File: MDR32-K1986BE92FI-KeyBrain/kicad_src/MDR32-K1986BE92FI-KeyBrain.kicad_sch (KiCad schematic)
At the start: 33 parts, among them J1 USB-C USB 2.0 MC-372, J2 Conn_01x04, U1 AP2112K-3.3, U2 USBLC6-2SC6, U3 K1986BE92FI, U4 ProMicro, Y1 8MHz

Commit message: MDR32-K1986BE92FI-KeyBrain: add usb fottprint
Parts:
- J1: footprint nrfmicro:USB-C_C168688 -> MDR32-K1986BE92FI-KeyBrain:USB-C_C168688
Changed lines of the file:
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@@
 			)
 		)
-		(property "Footprint" "nrfmicro:USB-C_C168688"
+		(property "Footprint" "MDR32-K1986BE92FI-KeyBrain:USB-C_C168688"
 			(at 31.9278 22.225 0)
 			(show_name no)

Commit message: MDR32-K1986BE92FI-KeyBrain: фикс символа кристалла
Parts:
- removed Y1: 8MHz, Crystal:Crystal_SMD_3225-4Pin_3.2x2.5mm, symbol MDR32-K1986BE92FI-DK:Crystal_GND24
- added Y1: 8MHz, Crystal:Crystal_SMD_3225-4Pin_3.2x2.5mm, symbol MDR32-K1986BE92FI-KeyBrain:Crystal_GND24
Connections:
- net GND: now also Y1.2 (G), Y1.4 (G)
- net OSC_IN: now also Y1.1
- net OSC_OUT: now also Y1.3
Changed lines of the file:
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@@
 	)
 	(junction
-		(at 78.74 127)
-		(diameter 0)
-		(color 0 0 0 0)
-	)
-	(junction
 		(at 46.99 44.45)
 		(diameter 0)
@@
 	(wire
 		(pts
-			(xy 78.74 125.73) (xy 78.74 127)
+			(xy 78.74 125.73) (xy 78.74 133.35)
 		)
 		(stroke
@@
 	(wire
 		(pts
-			(xy 78.74 127) (xy 83.82 127)
-		)
-		(stroke
-			(width 0)
-			(type default)
-		)
-	)
-	(wire
-		(pts
 			(xy 53.34 171.45) (xy 55.88 171.45)
 		)
@@
 	(wire
 		(pts
-			(xy 83.82 114.3) (xy 83.82 127)
-		)
-		(stroke
-			(width 0)
-			(type default)
-		)
-	)
-	(wire
-		(pts
 			(xy 52.07 34.29) (xy 52.07 46.99)
 		)
@@
 	(wire
 		(pts
-			(xy 78.74 114.3) (xy 83.82 114.3)
-		)
-		(stroke
-			(width 0)
-			(type default)
-		)
-	)
-	(wire
-		(pts
 			(xy 113.03 57.15) (xy 124.46 57.15)
 		)
@@
 	(wire
 		(pts
-			(xy 78.74 127) (xy 78.74 133.35)
-		)
-		(stroke
-			(width 0)
-			(type default)
-		)
-	)
-	(wire
-		(pts
 			(xy 143.51 173.99) (xy 143.51 179.07)
 		)
@@
 	(wire
 		(pts
-			(xy 78.74 115.57) (xy 78.74 114.3)
-		)
-		(stroke
-			(width 0)
-			(type default)
-		)
-	)
-	(wire
-		(pts
 			(xy 121.92 130.81) (xy 121.92 133.35)
 		)
@@
 	)
 	(symbol
+		(lib_id "MDR32-K1986BE92FI-KeyBrain:Crystal_GND24")
+		(at 78.74 120.65 0)
+		(unit 1)
+		(body_style 1)
+		(exclude_from_sim no)
+		(in_bom yes)
+		(on_board yes)
+		(in_pos_files yes)
+		(dnp no)
+		(fields_autoplaced yes)
+		(property "Reference" "Y1"
+			(at 78.74 111.76 0)
+			(show_name no)
+			(do_not_autoplace no)
+			(effects
+				(font
+					(size 1.27 1.27)
+				)
+			)
+		)
+		(property "Value" "8MHz"
+			(at 78.74 114.3 0)
+			(show_name no)
+			(do_not_autoplace no)
+			(effects
+				(font
+					(size 1.27 1.27)
+				)
+			)
+		)
+		(property "Footprint" "Crystal:Crystal_SMD_3225-4Pin_3.2x2.5mm"
+			(at 78.74 120.65 0)
+			(hide yes)
+			(show_name no)
+			(do_not_autoplace no)
+			(effects
+				(font
+					(size 1.27 1.27)
+				)
+			)
+		)
+		(property "Datasheet" ""
+			(at 78.74 120.65 0)
+			(hide yes)
+			(show_name no)
+			(do_not_autoplace no)
+			(effects
+				(font
+					(size 1.27 1.27)
+				)
+			)
+		)
+		(property "Description" "Four pin crystal, GND on pins 2 and 4"
+			(at 78.74 120.65 0)
+			(hide yes)
+			(show_name no)
+			(do_not_autoplace no)
+			(effects
+				(font
+					(size 1.27 1.27)
+				)
+			)
+		)
+		(property private "KLC_S3.3" "The rectangle is not a symbol body but a graphical element"
+			(at 78.74 133.35 0)
+			(hide yes)
+			(show_name yes)
+			(do_not_autoplace no)
+			(effects
+				(font
+					(size 1.27 1.27)
+				)
+			)
+		)
+		(property private "KLC_S4.1" "Some pins are on 50mil grid to make the symbol small"
+			(at 78.74 135.89 0)
+			(hide yes)
+			(show_name yes)
+			(do_not_autoplace no)
+			(effects
+				(font
+					(size 1.27 1.27)
+				)
+			)
+		)
+		(pin "1"
+		)
+		(pin "3"
+		)
+		(pin "4"
+		)
+		(pin "2"
+		)
+		(instances
+			(project "MDR32-K1986BE92FI-KeyBrain"
+				(path "/bfe5c5e1-24d1-41fe-819b-b49961f0f3b5"
+					(reference "Y1")
+					(unit 1)
+				)
+			)
+		)
+	)
+	(symbol
 		(lib_id "Device:C")
 		(at 24.13 177.8 0)
@@
 					(unit 1)
 				)
-			)
-		)
-	)
-	(symbol
-		(lib_id "MDR32-K1986BE92FI-DK:Crystal_GND24")
-		(at 78.74 120.65 0)
-		(unit 1)
-		(body_style 1)
-		(exclude_from_sim no)
-		(in_bom yes)
-		(on_board yes)
-		(in_pos_files yes)
-		(dnp no)
-		(property "Reference" "Y1"
-			(at 78.74 109.22 0)
-			(show_name no)
-			(do_not_autoplace no)
-			(effects
-				(font
-					(size 1.27 1.27)
-				)
-			)
-		)
-		(property "Value" "8MHz"
-			(at 78.74 111.76 0)
-			(show_name no)
-			(do_not_autoplace no)
-			(effects
-				(font
-					(size 1.27 1.27)
-				)
-			)
-		)
-		(property "Footprint" "Crystal:Crystal_SMD_3225-4Pin_3.2x2.5mm"
-			(at 78.74 120.65 0)
-			(hide yes)
-			(show_name no)
-			(do_not_autoplace no)
-			(effects
-				(font
-					(size 1.27 1.27)
-				)
-			)
-		)
-		(property "Datasheet" ""
-			(at 78.74 120.65 0)
-			(hide yes)
-			(show_name no)
-			(do_not_autoplace no)
-			(effects
-				(font
-					(size 1.27 1.27)
-				)
-			)
-		)
-		(property "Description" "Four pin crystal, GND on pins 2 and 4"
-			(at 78.74 120.65 0)
-			(hide yes)
-			(show_name no)
-			(do_not_autoplace no)
-			(effects
-				(font
-					(size 1.27 1.27)
-				)
-			)
-		)
-		(pin "4"
-		)
-		(pin "3"
-		)
-		(pin "1"
-		)
-		(pin "2"
-		)
-		(instances
-			(project "MDR32-K1986BE92FI-KeyBrain"
-				(path "/bfe5c5e1-24d1-41fe-819b-b49961f0f3b5"
-					(reference "Y1")
-					(unit 1)
-				)

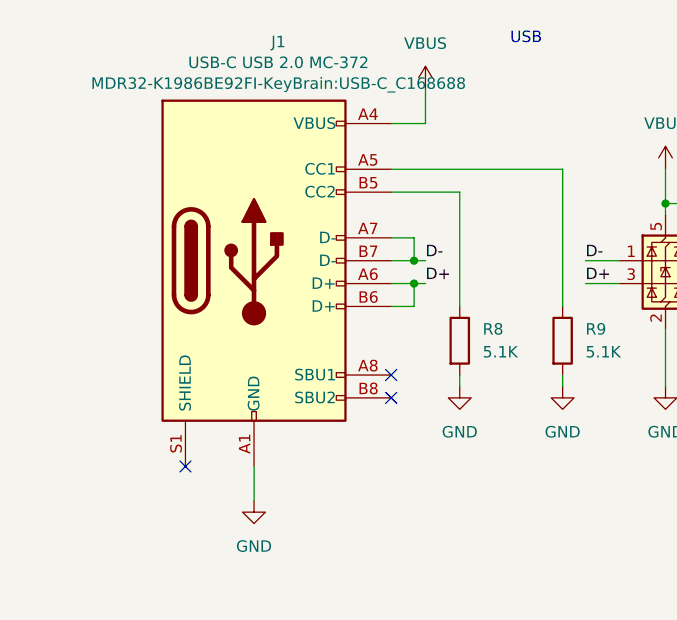
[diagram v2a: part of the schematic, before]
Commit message: MDR32-K1986BE92FI-KeyBrain: фикс символа USB
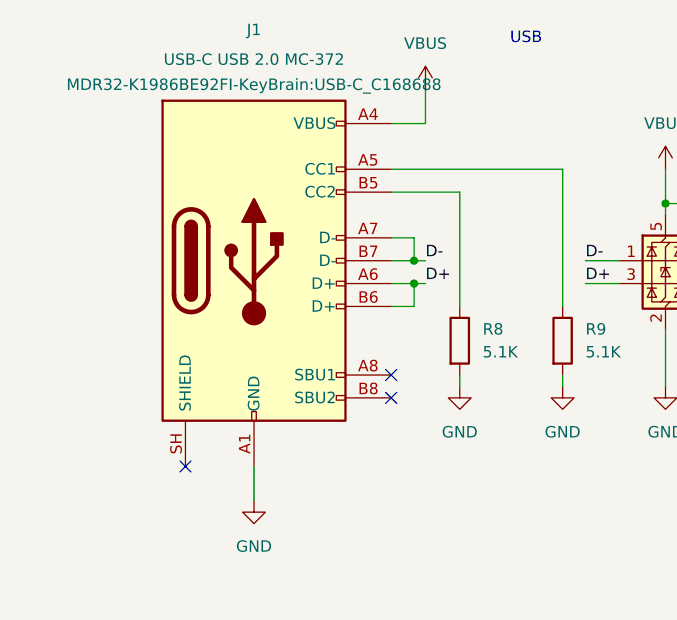
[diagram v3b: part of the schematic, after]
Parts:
- removed J1: USB-C USB 2.0 MC-372, MDR32-K1986BE92FI-KeyBrain:USB-C_C168688, symbol nrfmicro:USB_C_Receptacle_USB2.0
- added J1: USB-C USB 2.0 MC-372, MDR32-K1986BE92FI-KeyBrain:USB-C_C168688, symbol MDR32-K1986BE92FI-KeyBrain:USB_C_Receptacle_USB2.0_16P
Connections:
- net D+: now also J1.A6 (D+), J1.B6 (D+)
- net D-: now also J1.A7 (D-), J1.B7 (D-)
- net GND: now also J1.A1 (GND), J1.A12 (GND), J1.B1 (GND), J1.B12 (GND)
- net VBUS: now also J1.A4 (VBUS), J1.A9 (VBUS), J1.B4 (VBUS), J1.B9 (VBUS)
- net at R9.1: now also J1.A5 (CC1)
- net at R8.1: now also J1.B5 (CC2)
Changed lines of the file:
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@@
+	)
+	(symbol
+		(lib_id "MDR32-K1986BE92FI-KeyBrain:USB_C_Receptacle_USB2.0_16P")
+		(at 29.21 41.91 0)
+		(unit 1)
+		(body_style 1)
+		(exclude_from_sim no)
+		(in_bom yes)
+		(on_board yes)
+		(in_pos_files yes)
+		(dnp no)
+		(property "Reference" "J1"
+			(at 29.21 16.256 0)
+			(show_name no)
+			(do_not_autoplace no)
+			(effects
+				(font
+					(size 1.27 1.27)
+				)
+			)
+		)
+		(property "Value" "USB-C USB 2.0 MC-372"
+			(at 29.21 19.558 0)
+			(show_name no)
+			(do_not_autoplace no)
+			(effects
+				(font
+					(size 1.27 1.27)
+				)
+			)
+		)
+		(property "Footprint" "MDR32-K1986BE92FI-KeyBrain:USB-C_C168688"
+			(at 29.21 22.352 0)
+			(show_name no)
+			(do_not_autoplace no)
+			(effects
+				(font
+					(size 1.27 1.27)
+				)
+			)
+		)
+		(property "Datasheet" "https://www.usb.org/sites/default/files/documents/usb_type-c.zip"
+			(at 33.02 41.91 0)
+			(hide yes)
+			(show_name no)
+			(do_not_autoplace no)
+			(effects
+				(font
+					(size 1.27 1.27)
+				)
+			)
+		)
+		(property "Description" "USB 2.0-only 16P Type-C Receptacle connector"
+			(at 29.21 41.91 0)
+			(hide yes)
+			(show_name no)
+			(do_not_autoplace no)
+			(effects
+				(font
+					(size 1.27 1.27)
+				)
+			)
+		)
+		(pin "A7"
+		)
+		(pin "A6"
+		)
+		(pin "A5"
+		)
+		(pin "A4"
+		)
+		(pin "A1"
+		)
+		(pin "B6"
+		)
+		(pin "B7"
+		)
+		(pin "B12"
+		)
+		(pin "B8"
+		)
+		(pin "A8"
+		)
+		(pin "A9"
+		)
+		(pin "B9"
+		)
+		(pin "B5"
+		)
+		(pin "B4"
+		)
+		(pin "B1"
+		)
+		(pin "A12"
+		)
+		(pin "SH"
+		)
+		(instances
+			(project "MDR32-K1986BE92FI-KeyBrain"
+				(path "/bfe5c5e1-24d1-41fe-819b-b49961f0f3b5"
+					(reference "J1")
+					(unit 1)
+				)
+			)
+		)
 	)
 	(symbol
@@
 					(unit 1)
 				)
-			)
-		)
-	)
-	(symbol
-		(lib_id "nrfmicro:USB_C_Receptacle_USB2.0")
-		(at 29.21 41.91 0)
-		(unit 1)
-		(body_style 1)
-		(exclude_from_sim no)
-		(in_bom yes)
-		(on_board yes)
-		(in_pos_files yes)
-		(dnp no)
-		(property "Reference" "J1"
-			(at 31.9278 17.6022 0)
-			(show_name no)
-			(do_not_autoplace no)
-			(effects
-				(font
-					(size 1.27 1.27)
-				)
-			)
-		)
-		(property "Value" "USB-C USB 2.0 MC-372"
-			(at 31.9278 19.9136 0)
-			(show_name no)
-			(do_not_autoplace no)
-			(effects
-				(font
-					(size 1.27 1.27)
-				)
-			)
-		)
-		(property "Footprint" "MDR32-K1986BE92FI-KeyBrain:USB-C_C168688"
-			(at 31.9278 22.225 0)
-			(show_name no)
-			(do_not_autoplace no)
-			(effects
-				(font
-					(size 1.27 1.27)
-				)
-			)
-		)
-		(property "Datasheet" "https://www.usb.org/sites/default/files/documents/usb_type-c.zip"
-			(at 33.02 41.91 0)
-			(hide yes)
-			(show_name no)
-			(do_not_autoplace no)
-			(effects
-				(font
-					(size 1.27 1.27)
-				)
-			)
-		)
-		(property "Description" ""
-			(at 29.21 41.91 0)
-			(show_name no)
-			(do_not_autoplace no)
-			(effects
-				(font
-					(size 1.27 1.27)
-				)
-			)
-		)
-		(pin "A1"
-		)
-		(pin "A4"
-		)
-		(pin "A5"
-		)
-		(pin "A6"
-		)
-		(pin "A7"
-		)
-		(pin "B5"
-		)
-		(pin "B6"
-		)
-		(pin "B7"
-		)
-		(pin "S1"
-		)
-		(pin "A8"
-		)
-		(pin "B8"
-		)
-		(instances
-			(project "MDR32-K1986BE92FI-KeyBrain"
-				(path "/bfe5c5e1-24d1-41fe-819b-b49961f0f3b5"
-					(reference "J1")
-					(unit 1)
-				)

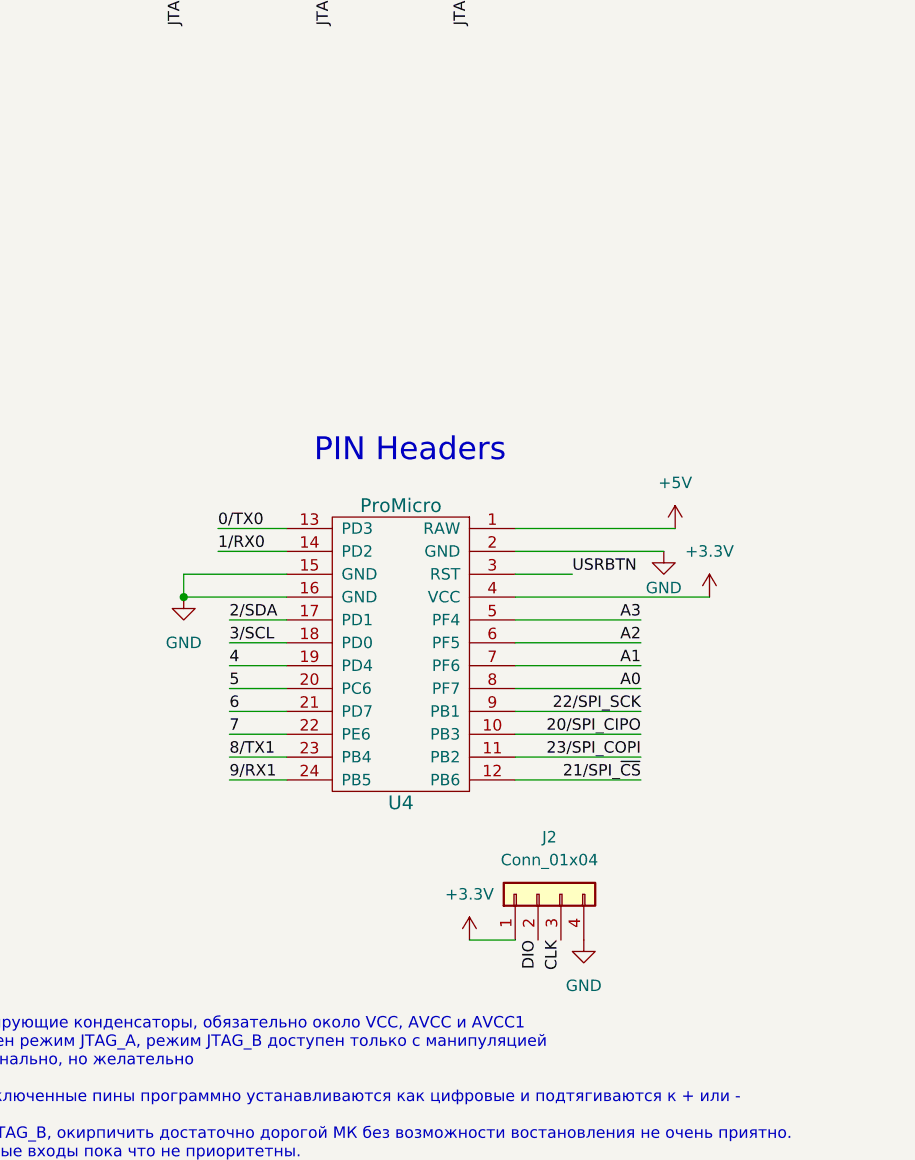
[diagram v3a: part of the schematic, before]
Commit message: MDR32-K1986BE92FI-KeyBrain: fix символа ProMicro
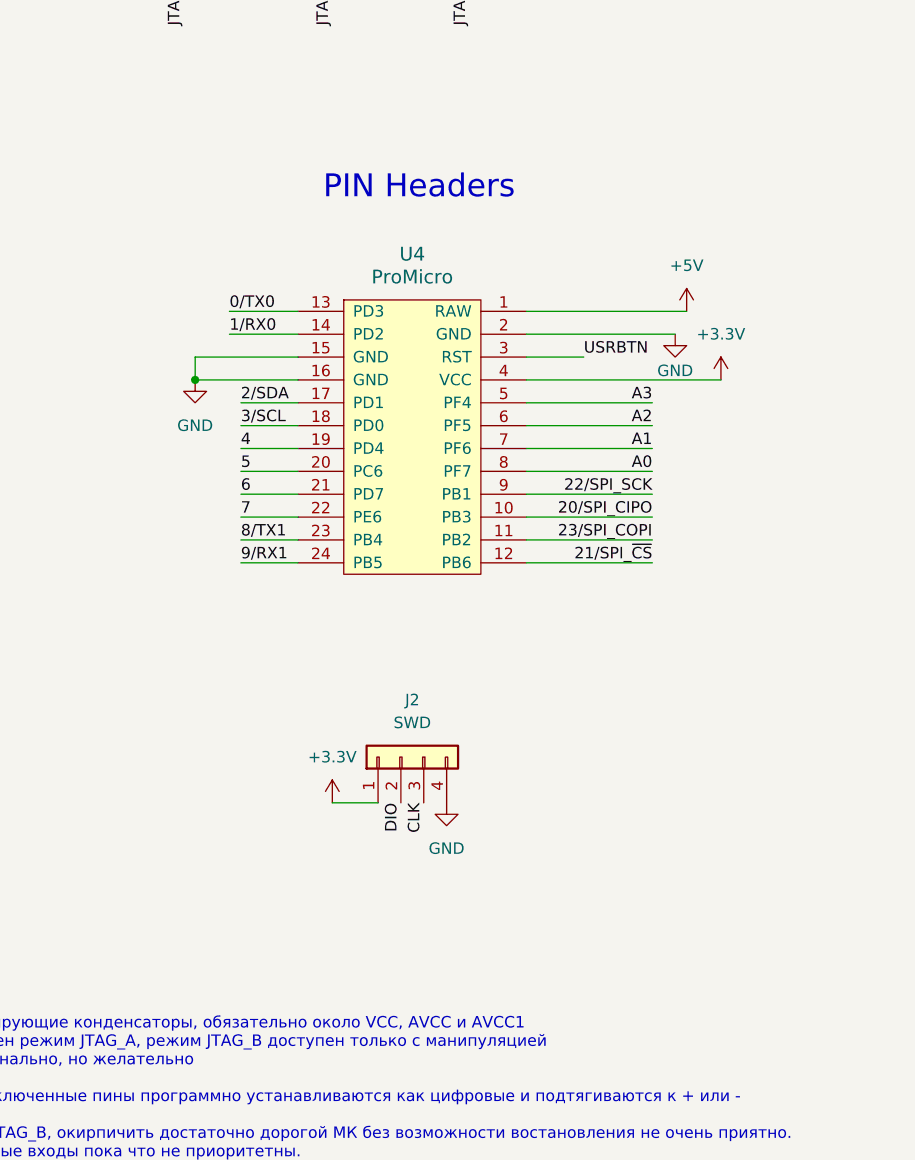
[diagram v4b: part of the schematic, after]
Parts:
- removed U4: ProMicro, nrfmicro:pro_micro, symbol nrfmicro-rescue:ProMicro
- added U4: ProMicro, MDR32-K1986BE92FI-KeyBrain:pro_micro, symbol MDR32-K1986BE92FI-KeyBrain:ProMicro
- J2: value Conn_01x04 -> SWD
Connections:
- net +3.3V: now also U4.4 (VCC)
- net +5V: now also U4.1 (RAW)
- net 0/TX0: now also U4.13 (PD3)
- net 1/RX0: now also U4.14 (PD2)
- net 20/SPI_CIPO: now also U4.10 (PB3)
- net 21/SPI_~{CS}: now also U4.12 (PB6)
- net 22/SPI_SCK: now also U4.9 (PB1)
- net 23/SPI_COPI: now also U4.11 (PB2)
- net 2/SDA: now also U4.17 (PD1)
- net 3/SCL: now also U4.18 (PD0)
- net 4: now also U4.19 (PD4)
- net 5: now also U4.20 (PC6)
- net 6: now also U4.21 (PD7)
- net 7: now also U4.22 (PE6)
- net 8/TX1: now also U4.23 (PB4)
- net 9/RX1: now also U4.24 (PB5)
- net A0: now also U4.8 (PF7)
- net A1: now also U4.7 (PF6)
- net A2: now also U4.6 (PF5)
- net A3: now also U4.5 (PF4)
- net GND: now also U4.15 (GND), U4.16 (GND), U4.2 (GND)
- net USRBTN: now also U4.3 (RST)
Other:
- moved on the sheet: J2
